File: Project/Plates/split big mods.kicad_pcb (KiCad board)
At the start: 2 copper layers, 257.2 x 76.2 mm, 46 parts

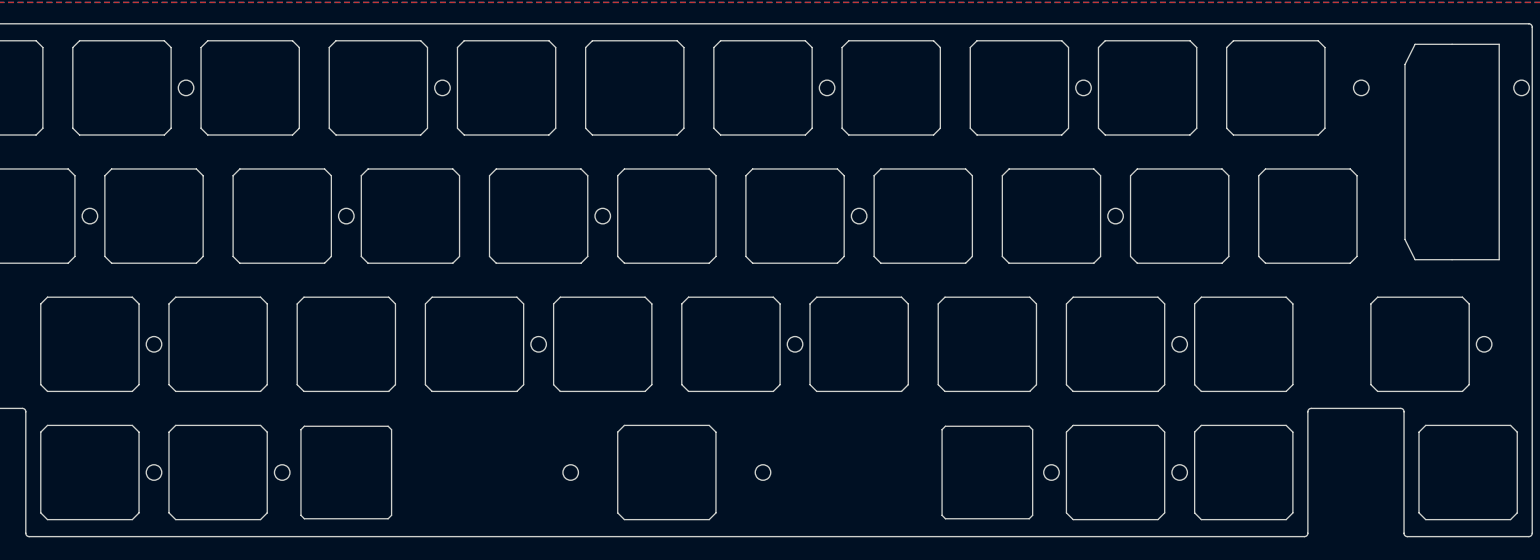
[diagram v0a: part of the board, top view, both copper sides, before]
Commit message: bottom row change, plate update, firmware update
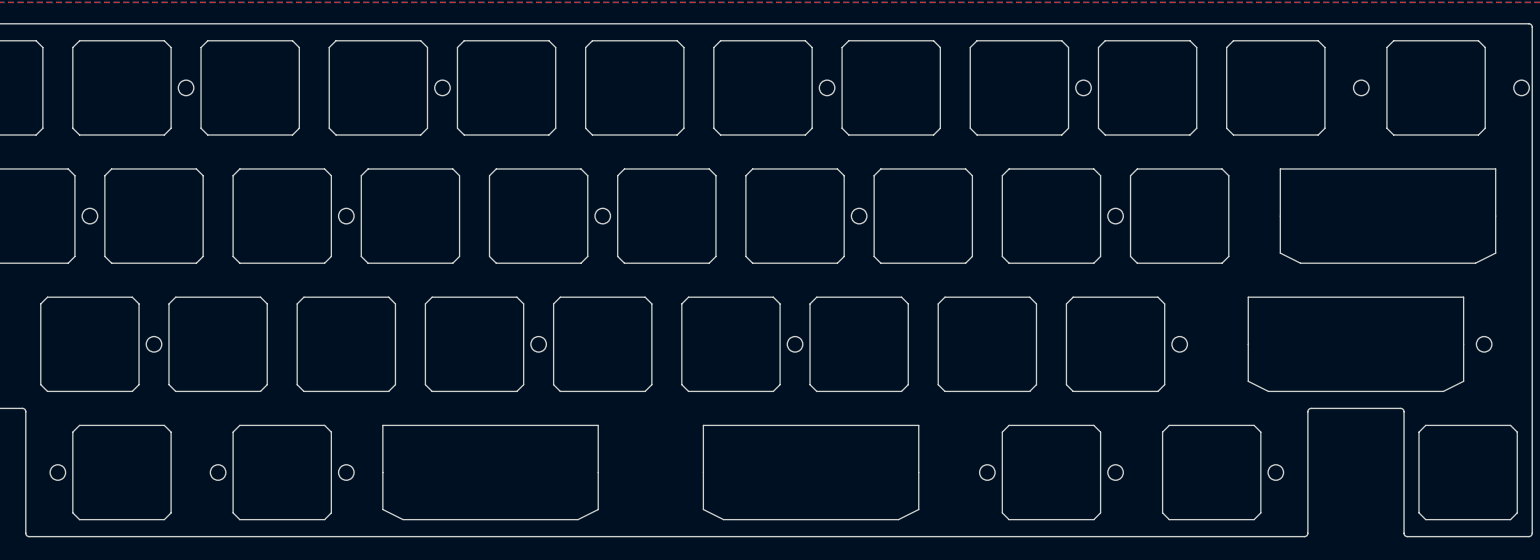
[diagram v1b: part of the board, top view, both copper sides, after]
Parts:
- removed the REF** at (146.1, 91.3) (x3)
- removed the REF** at (79.4, 91.3)
- removed the REF** at (212.7, 91.3)
- removed the REF** at (258.0, 72.2)
- removed the REF** at (231.8, 72.2)
- removed the REF** at (60.3, 91.3)
- removed the REF** at (262.7, 43.7)
- removed the REF** at (241.3, 53.2)
- removed the REF** at (231.8, 91.3)
- added REF**: Value, cipulot_parts:ecs_plate_cut_1U, F.Cu at (88.9, 91.3)
- added REF**: Value, cipulot_parts:ecs_plate_cut_1U, F.Cu at (203.2, 91.3)
- added REF**: Value, cipulot_parts:ecs_plate_cut_2U, F.Cu at (248.4, 72.2)
- added REF**: Value, cipulot_parts:ecs_plate_cut_2U, F.Cu at (119.9, 91.3)
- added REF**: Value, cipulot_parts:ecs_plate_cut_2U, F.Cu at (253.2, 53.2)
- added REF**: Value, cipulot_parts:ecs_plate_cut_2U, F.Cu at (167.5, 91.3)
- added REF**: Value, cipulot_parts:ecs_plate_cut_1U, F.Cu at (65.1, 91.3)
- added REF**: Value, cipulot_parts:ecs_plate_cut_1U, F.Cu at (227.0, 91.3)
- added REF**: Value, cipulot_parts:ecs_plate_cut_1U, F.Cu at (260.4, 34.1)
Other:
- outline, holes or cut-outs redrawn
- board text removed: "REF**"
